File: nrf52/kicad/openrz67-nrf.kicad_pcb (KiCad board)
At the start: 2 copper layers, 31 x 30 mm, 13 parts, among them J1 Camera, J2 SWD, SW1 B3U-1000P, U1 E73-2G4M08S1C, U2 TLP172AM, U3 TLP172AM

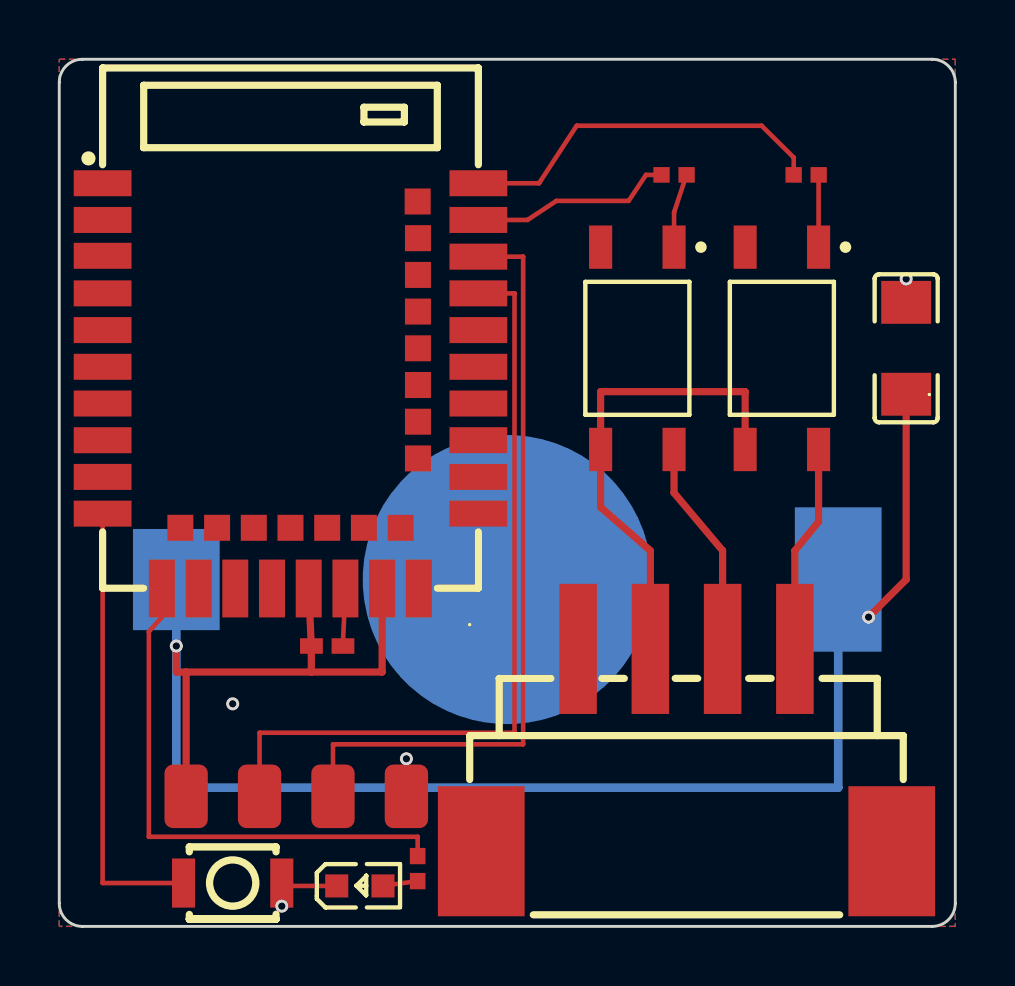
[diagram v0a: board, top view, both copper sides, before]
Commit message: nrf52: JST SH camera connector, datasheet facts
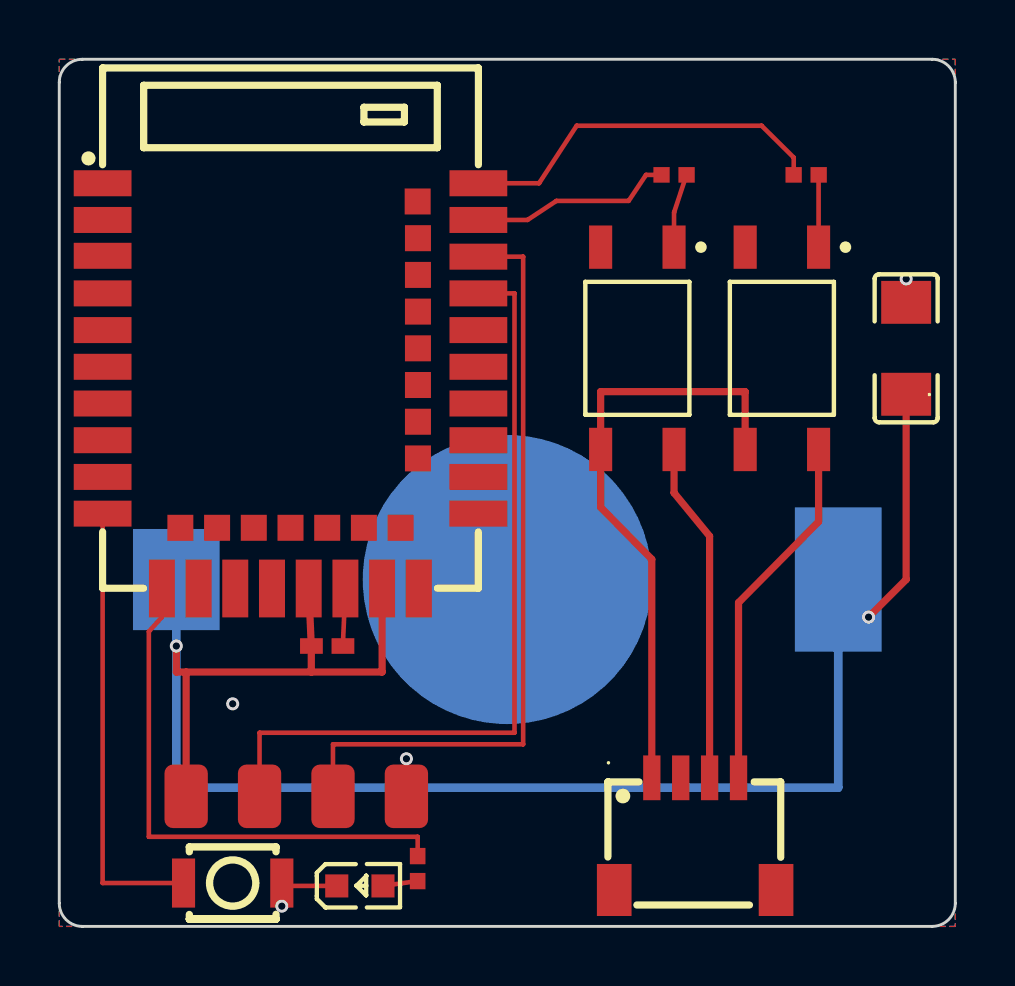
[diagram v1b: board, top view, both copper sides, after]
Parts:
- J1: footprint openrz67-nrf:CONN-SMD_S4B-XH-SM4-TB-LF-SN -> openrz67-nrf:CONN-SMD_4P-P1.00_SM04B-SRSS-TB-LF-SN
- moved J1 2.92 mm to (22.0, 26.8)
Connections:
- J1 pad 1: unconnected-(J1-Pad1) -> CAM_GND
- J1 pad 2: CAM_GND -> unconnected-(J1-Pad2)
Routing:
- net S2: track 4.99 -> 11.7 mm
- net CAM_GND: track 14.5 -> 20.3 mm
- net S1: track 5.31 -> 11.0 mm

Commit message: nrf52: board 27 x 29
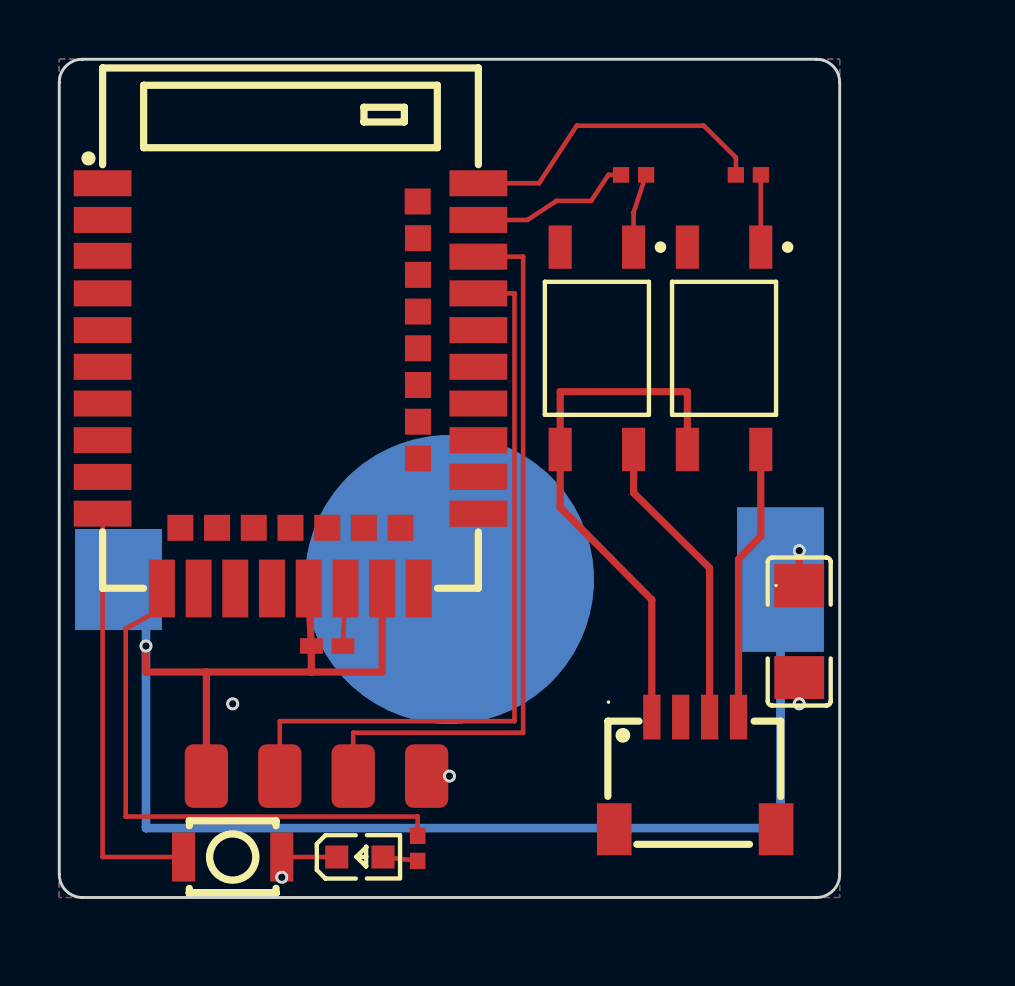
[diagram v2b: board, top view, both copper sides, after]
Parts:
- moved C1 10.5 mm to (25.6, 19.8), turned to -90 degrees
- moved J1 2.10 mm to (22.0, 24.7)
- moved BT1 2.00 mm to (13.5, 18.0)
- moved R2 2.00 mm to (23.8, 4.00)
- moved U3 2.00 mm to (23.0, 10.0)
- moved R1 1.40 mm to (19.9, 4.00)
- moved U2 1.40 mm to (18.6, 10.0)
- moved D1 1.00 mm to (10.4, 27.6)
- moved J2 0.99 mm to (8.90, 24.8)
- moved SW1 0.90 mm to (6.00, 27.6)
- moved R3 0.70 mm to (12.4, 27.3)
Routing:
- net VDD: track 60.9 -> 54.7 mm
- net S2: track 11.7 -> 8.81 mm
- net CAM_GND: track 20.3 -> 18.2 mm
- net S2_DRV: track 13.0 -> 11.0 mm
- net S1: track 11.0 -> 9.60 mm
- net SWDIO: track 26.4 -> 25.0 mm
- net SWCLK: track 25.7 -> 24.3 mm
- net S1_DRV: track 7.02 -> 5.62 mm
- net BTN: track 15.6 -> 14.7 mm
- net LED_DRV: track 18.7 -> 19.4 mm
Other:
- board size 31 x 30 mm -> 27 x 29 mm

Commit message: nrf52: case first pass
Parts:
- moved C1 2.80 mm to (25.6, 17.0)
- moved D1 1.60 mm to (12.0, 27.6)
- moved R3 1.60 mm to (14.0, 27.3)
- moved J1 0.70 mm to (21.3, 24.7)
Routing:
- net GND: track 3.49 -> 7.50 mm
- net LED_DRV: track 19.4 -> 21.0 mm
- net VDD: track 54.7 -> 54.0 mm

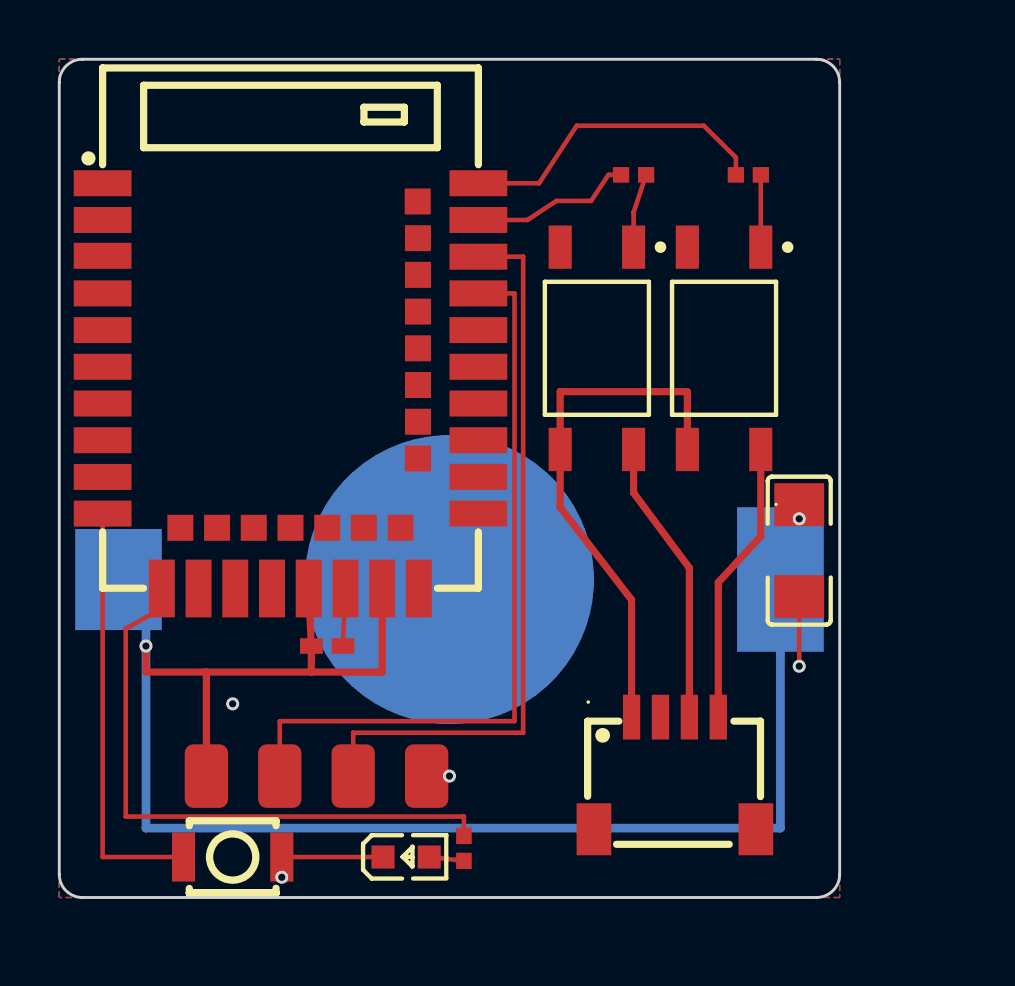
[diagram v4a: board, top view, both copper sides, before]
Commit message: nrf52: SH connector for SWD, parts list
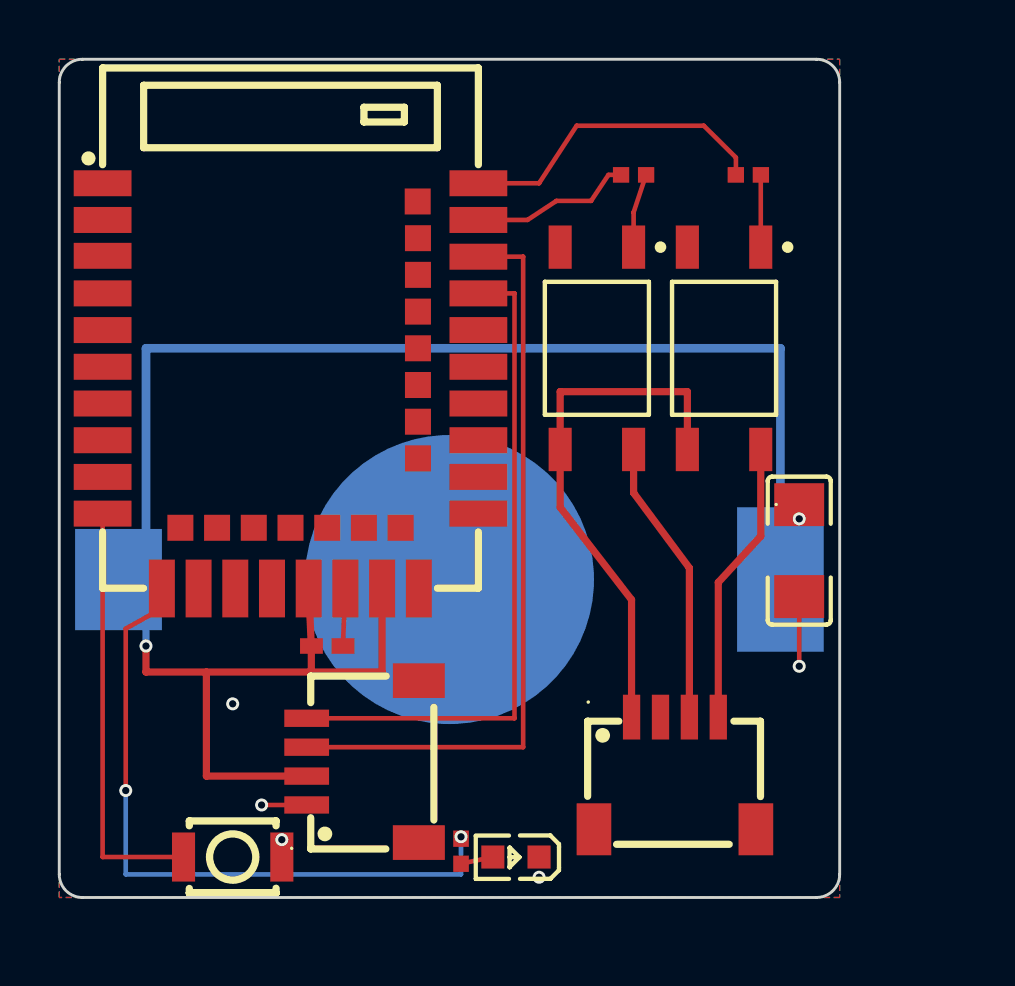
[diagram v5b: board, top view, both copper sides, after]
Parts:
- J2: footprint openrz67-nrf:SWD_1x04_P2.54 -> openrz67-nrf:CONN-SMD_4P-P1.00_SM04B-SRSS-TB-LF-SN
- moved D1 3.80 mm to (15.8, 27.6), turned to 180 degrees
- moved J2 1.68 mm to (10.5, 24.3), turned to 90 degrees
- moved R3 0.14 mm to (13.9, 27.4)
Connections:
- J2 pad 1: VDD -> GND
- J2 pad 2: SWDIO -> VDD
- J2 pad 4: GND -> SWDIO
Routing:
- net VDD: track 54.0 -> 56.7 mm
- net SWDIO: track 25.0 -> 22.4 mm
- net LED_DRV: track 21.0 -> 23.5 mm, vias 0 -> 2
- net GND: track 7.50 -> 5.18 mm, vias 4 -> 5
- net SWCLK: track 24.3 -> 25.2 mm

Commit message: nrf52: review fixes before ordering
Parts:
- turned R3 to 90 degrees
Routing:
- net VDD: track 56.7 -> 65.7 mm
- net GND: track 5.18 -> 5.88 mm, vias 5 -> 9
